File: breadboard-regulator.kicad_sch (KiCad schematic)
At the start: 16 parts, among them J1 Barrel_Jack_Switch, U1 LM7805_TO220, U2 LD1117S33TR_SOT223

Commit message: finish schematic and PCB design
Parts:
- added J2, J3: Conn_01x02_Pin, Connector_PinHeader_2.54mm:PinHeader_1x02_P2.54mm_Vertical, symbol Connector:Conn_01x02_Pin
- U2: value LD1117S33TR_SOT223 -> LD1117V33_TO-220
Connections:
- net +3.3V: now also J3.1 (Pin_1)
- net +5V: now also J2.1 (Pin_1)
- net GND: now also D2.1 (K), D3.1 (K), J2.2 (Pin_2), J3.2 (Pin_2)
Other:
- moved on the sheet: D2, D3, R1, R2

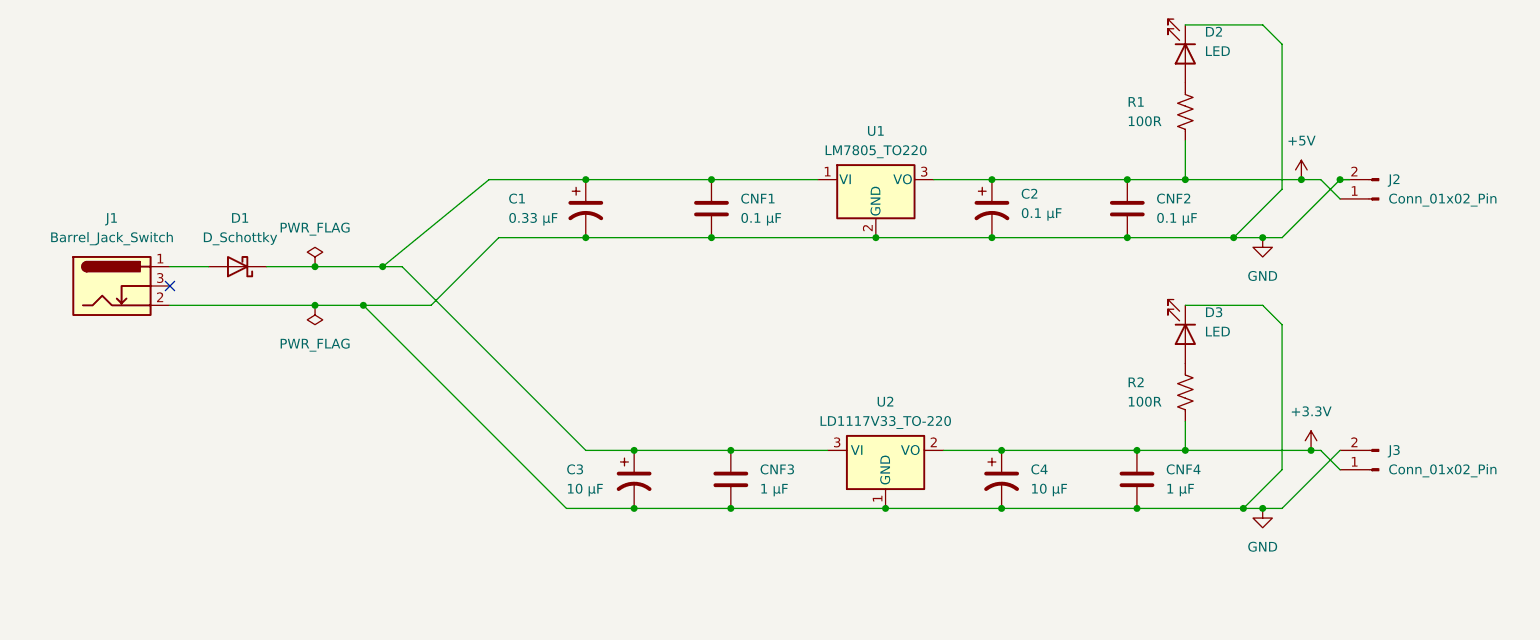
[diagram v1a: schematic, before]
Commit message: split schematics diagram; rearrange PCB
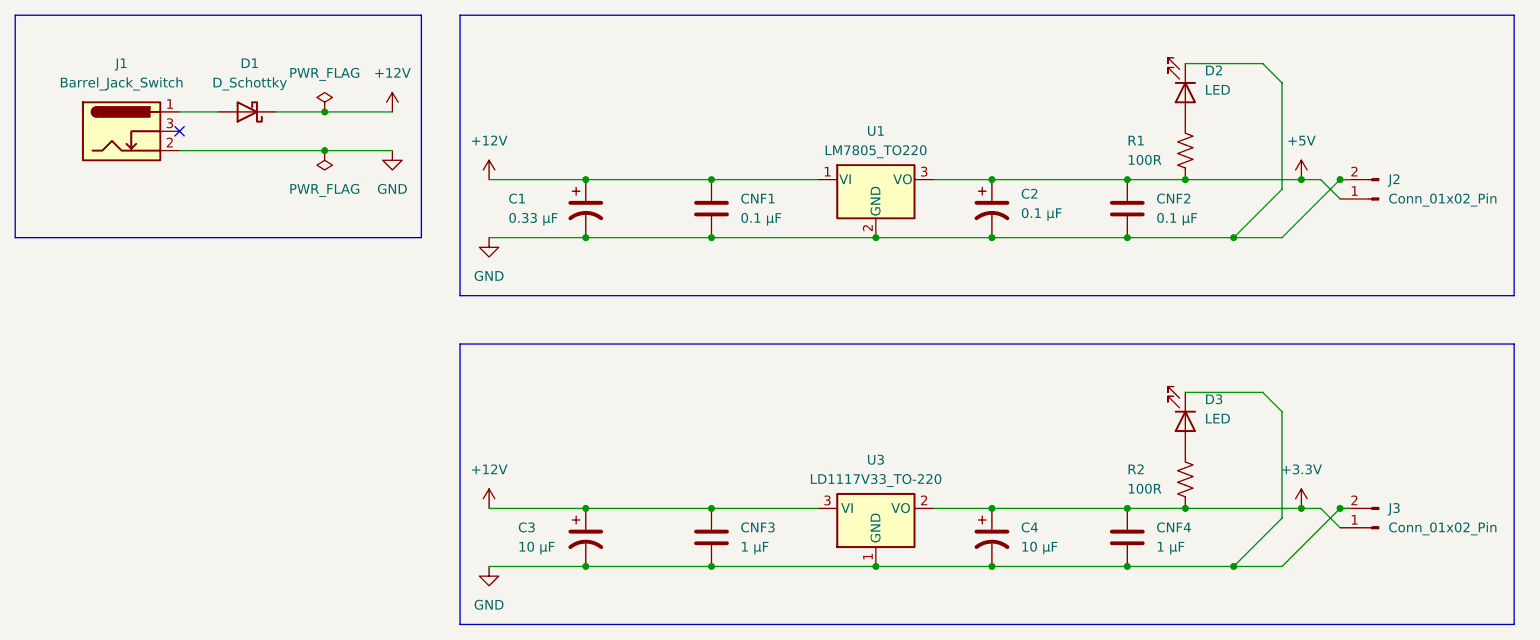
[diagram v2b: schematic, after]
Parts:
- removed U2: LD1117V33_TO-220, Package_TO_SOT_THT:TO-220-3_Vertical, symbol Regulator_Linear:LD1117S33TR_SOT223
- added U3: LD1117V33_TO-220, Package_TO_SOT_THT:TO-220-3_Vertical, symbol Regulator_Linear:LD1117S33TR_SOT223
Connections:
- net +3.3V: now also U3.2 (VO)
- net GND: now also U3.1 (GND)
- net +12V: now reaches C1.1, C3.1, CNF1.1, CNF3.1, D1.1 (K), U1.1 (VI)
- net +12V: now also U3.3 (VI)
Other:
- moved on the sheet: D1, D2, J1, R1

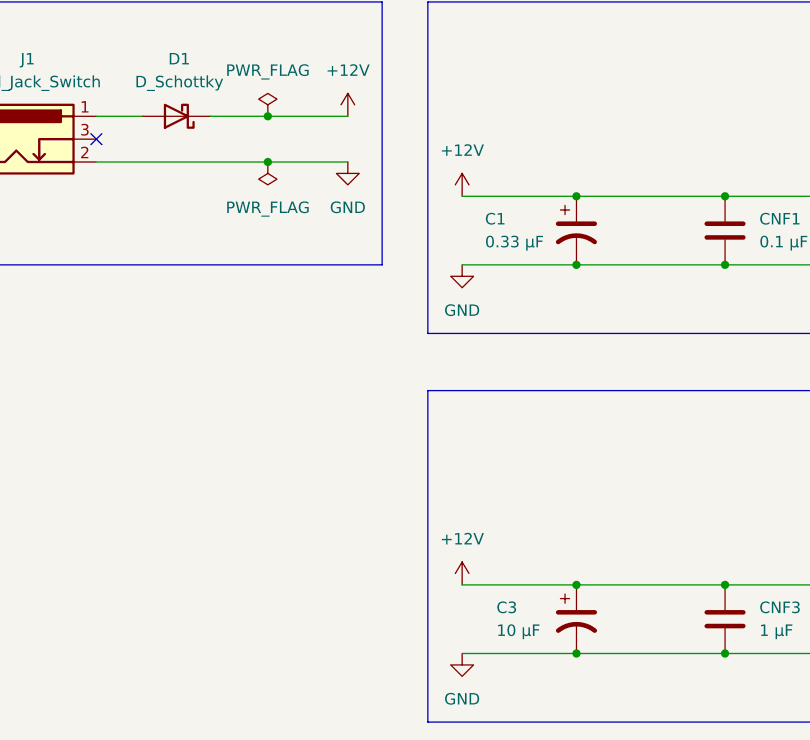
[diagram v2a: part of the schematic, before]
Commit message: change from GND to GNDREF
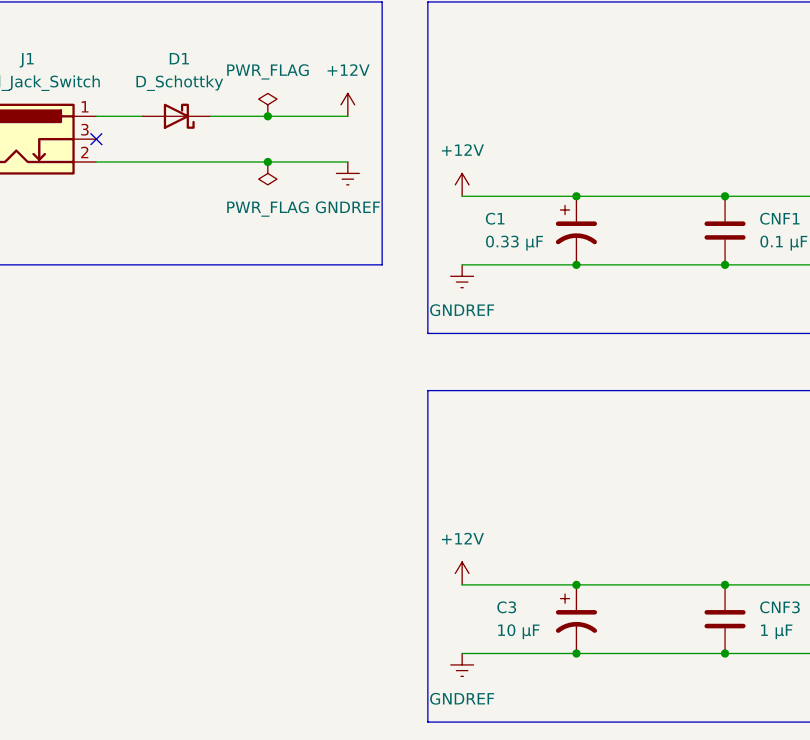
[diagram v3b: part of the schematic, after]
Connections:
- net GND renamed GNDREF
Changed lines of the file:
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@@
-    )
-  )
-  (symbol (lib_id "power:GND") (at 87.63 50.8 0) (unit 1)
-    (in_bom yes) (on_board yes) (dnp no) (fields_autoplaced)
-    (property "Reference" "#PWR06" (at 87.63 57.15 0)
-      (effects (font (size 1.27 1.27)) hide)
-    )
-    (property "Value" "GND" (at 87.63 55.88 0)
-      (effects (font (size 1.27 1.27)))
-    )
-    (property "Footprint" "" (at 87.63 50.8 0)
-      (effects (font (size 1.27 1.27)) hide)
-    )
-    (property "Datasheet" "" (at 87.63 50.8 0)
-      (effects (font (size 1.27 1.27)) hide)
-    )
-    (pin "1")
-    (instances
-      (project "breadboard-regulator"
-        (path "/6c69cf60-5166-477a-bd3a-75a53b81548c"
-          (reference "#PWR06") (unit 1)
-        )
-      )
     )
   )
@@
     )
   )
-  (symbol (lib_id "power:GND") (at 100.33 62.23 0) (unit 1)
-    (in_bom yes) (on_board yes) (dnp no) (fields_autoplaced)
-    (property "Reference" "#PWR08" (at 100.33 68.58 0)
-      (effects (font (size 1.27 1.27)) hide)
-    )
-    (property "Value" "GND" (at 100.33 67.31 0)
-      (effects (font (size 1.27 1.27)))
-    )
-    (property "Footprint" "" (at 100.33 62.23 0)
-      (effects (font (size 1.27 1.27)) hide)
-    )
-    (property "Datasheet" "" (at 100.33 62.23 0)
+  (symbol (lib_id "power:GNDREF") (at 100.33 105.41 0) (unit 1)
+    (in_bom yes) (on_board yes) (dnp no) (fields_autoplaced)
+    (property "Reference" "#PWR08" (at 100.33 111.76 0)
+      (effects (font (size 1.27 1.27)) hide)
+    )
+    (property "Value" "GNDREF" (at 100.33 110.49 0)
+      (effects (font (size 1.27 1.27)))
+    )
+    (property "Footprint" "" (at 100.33 105.41 0)
+      (effects (font (size 1.27 1.27)) hide)
+    )
+    (property "Datasheet" "" (at 100.33 105.41 0)
       (effects (font (size 1.27 1.27)) hide)
     )
@@
         (path "/6c69cf60-5166-477a-bd3a-75a53b81548c"
           (reference "#PWR08") (unit 1)
+        )
+      )
+    )
+  )
+  (symbol (lib_id "power:GNDREF") (at 87.63 50.8 0) (unit 1)
+    (in_bom yes) (on_board yes) (dnp no) (fields_autoplaced)
+    (property "Reference" "#PWR02" (at 87.63 57.15 0)
+      (effects (font (size 1.27 1.27)) hide)
+    )
+    (property "Value" "GNDREF" (at 87.63 55.88 0)
+      (effects (font (size 1.27 1.27)))
+    )
+    (property "Footprint" "" (at 87.63 50.8 0)
+      (effects (font (size 1.27 1.27)) hide)
+    )
+    (property "Datasheet" "" (at 87.63 50.8 0)
+      (effects (font (size 1.27 1.27)) hide)
+    )
+    (pin "1")
+    (instances
+      (project "breadboard-regulator"
+        (path "/6c69cf60-5166-477a-bd3a-75a53b81548c"
+          (reference "#PWR02") (unit 1)
         )
       )
@@
     )
   )
+  (symbol (lib_id "power:GNDREF") (at 100.33 62.23 0) (unit 1)
+    (in_bom yes) (on_board yes) (dnp no) (fields_autoplaced)
+    (property "Reference" "#PWR06" (at 100.33 68.58 0)
+      (effects (font (size 1.27 1.27)) hide)
+    )
+    (property "Value" "GNDREF" (at 100.33 67.31 0)
+      (effects (font (size 1.27 1.27)))
+    )
+    (property "Footprint" "" (at 100.33 62.23 0)
+      (effects (font (size 1.27 1.27)) hide)
+    )
+    (property "Datasheet" "" (at 100.33 62.23 0)
+      (effects (font (size 1.27 1.27)) hide)
+    )
+    (pin "1")
+    (instances
+      (project "breadboard-regulator"
+        (path "/6c69cf60-5166-477a-bd3a-75a53b81548c"
+          (reference "#PWR06") (unit 1)
+        )
+      )
+    )
+  )
   (symbol (lib_id "Device:C_Polarized_US") (at 166.37 58.42 0) (unit 1)
     (in_bom yes) (on_board yes) (dnp no) (fields_autoplaced)
@@
         )
       )
-    )
-  )
-  (symbol (lib_id "power:GND") (at 100.33 105.41 0) (unit 1)
-    (in_bom yes) (on_board yes) (dnp no) (fields_autoplaced)
-    (property "Reference" "#PWR09" (at 100.33 111.76 0)
-      (effects (font (size 1.27 1.27)) hide)
-    )
-    (property "Value" "GND" (at 100.33 110.49 0)
-      (effects (font (size 1.27 1.27)))
-    )
-    (property "Footprint" "" (at 100.33 105.41 0)
-      (effects (font (size 1.27 1.27)) hide)
-    )
-    (property "Datasheet" "" (at 100.33 105.41 0)
-      (effects (font (size 1.27 1.27)) hide)
-    )
-    (pin "1")
-    (instances
-      (project "breadboard-regulator"
-        (path "/6c69cf60-5166-477a-bd3a-75a53b81548c"
-          (reference "#PWR09") (unit 1)
-        )
-      )

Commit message: add new beginner pin header
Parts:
- D2, D3: footprint BeginnerModules:BeginnerLED_D5.0mm -> BeginnerModules:LED_D5.0mm
- J2, J3: footprint Connector_PinHeader_2.54mm:PinHeader_1x02_P2.54mm_Vertical -> BeginnerModules:PinHeader_1x02_P2.54mm_Vertical
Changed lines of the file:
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@@
       (effects (font (size 1.27 1.27)) (justify left))
     )
-    (property "Footprint" "BeginnerModules:BeginnerLED_D5.0mm" (at 191.77 86.36 0)
+    (property "Footprint" "BeginnerModules:LED_D5.0mm" (at 191.77 86.36 0)
       (effects (font (size 1.27 1.27)) hide)
     )
@@
       (effects (font (size 1.27 1.27)) (justify left))
     )
-    (property "Footprint" "BeginnerModules:BeginnerLED_D5.0mm" (at 191.77 43.18 0)
+    (property "Footprint" "BeginnerModules:LED_D5.0mm" (at 191.77 43.18 0)
       (effects (font (size 1.27 1.27)) hide)
     )
@@
       (effects (font (size 1.27 1.27)) (justify right))
     )
-    (property "Footprint" "Connector_PinHeader_2.54mm:PinHeader_1x02_P2.54mm_Vertical" (at 217.17 100.33 0)
+    (property "Footprint" "BeginnerModules:PinHeader_1x02_P2.54mm_Vertical" (at 217.17 100.33 0)
       (effects (font (size 1.27 1.27)) hide)
     )
@@
       (effects (font (size 1.27 1.27)) (justify right))
     )
-    (property "Footprint" "Connector_PinHeader_2.54mm:PinHeader_1x02_P2.54mm_Vertical" (at 217.17 57.15 0)
-      (effects (font (size 1.27 1.27)) hide)
-    )
+    (property "Footprint" "BeginnerModules:PinHeader_1x02_P2.54mm_Vertical" (at 217.17 57.15 0)
+      (effects (font (size 1.27 1.27)) hide)
+    )

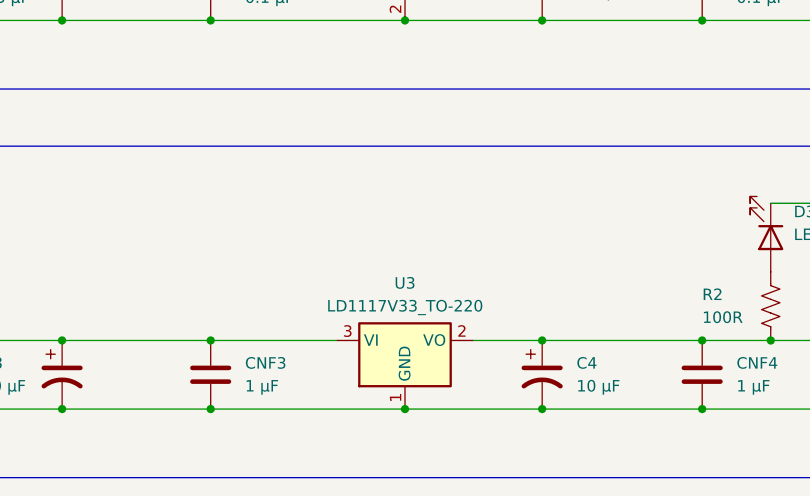
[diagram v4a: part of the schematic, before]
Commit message: change reference name
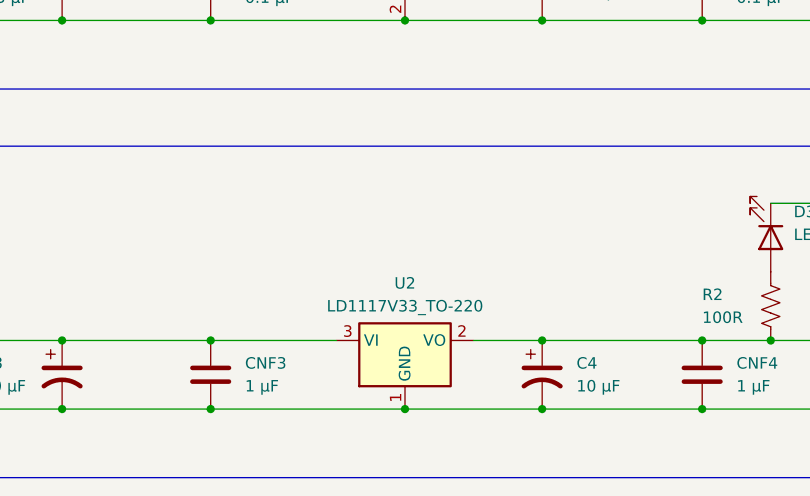
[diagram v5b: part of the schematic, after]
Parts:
- renumbered U3 to U2
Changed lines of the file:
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@@
   (symbol (lib_id "Regulator_Linear:LD1117S33TR_SOT223") (at 151.13 97.79 0) (unit 1)
     (in_bom yes) (on_board yes) (dnp no) (fields_autoplaced)
-    (property "Reference" "U3" (at 151.13 91.44 0)
+    (property "Reference" "U2" (at 151.13 91.44 0)
       (effects (font (size 1.27 1.27)))
     )
@@
       (project "breadboard-regulator"
         (path "/6c69cf60-5166-477a-bd3a-75a53b81548c"
-          (reference "U3") (unit 1)
+          (reference "U2") (unit 1)
         )
       )
